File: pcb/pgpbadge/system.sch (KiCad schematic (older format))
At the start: 29 parts

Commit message: Board layout and routing done, need to fix DRC's, add more ground stitching, clean up silscreen, and review
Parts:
- added VIB+1: VIB+, pgpbadge:solder_pad, symbol Connector_Generic:Conn_01x01
- added VIB-1: VIB-, pgpbadge:solder_pad, symbol Connector_Generic:Conn_01x01
- gave numbers to parts that had none: 28
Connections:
- net En: now also C14.2, R16.2, U5.3 (EN)
- net GND: now also VIB-1.1 (Pin_1)
- net VIBPWM: now also VIB+1.1 (Pin_1)
- net GPOUT: no longer names the net of U5.27 (IO16)
- no-connect marks 13 -> 26

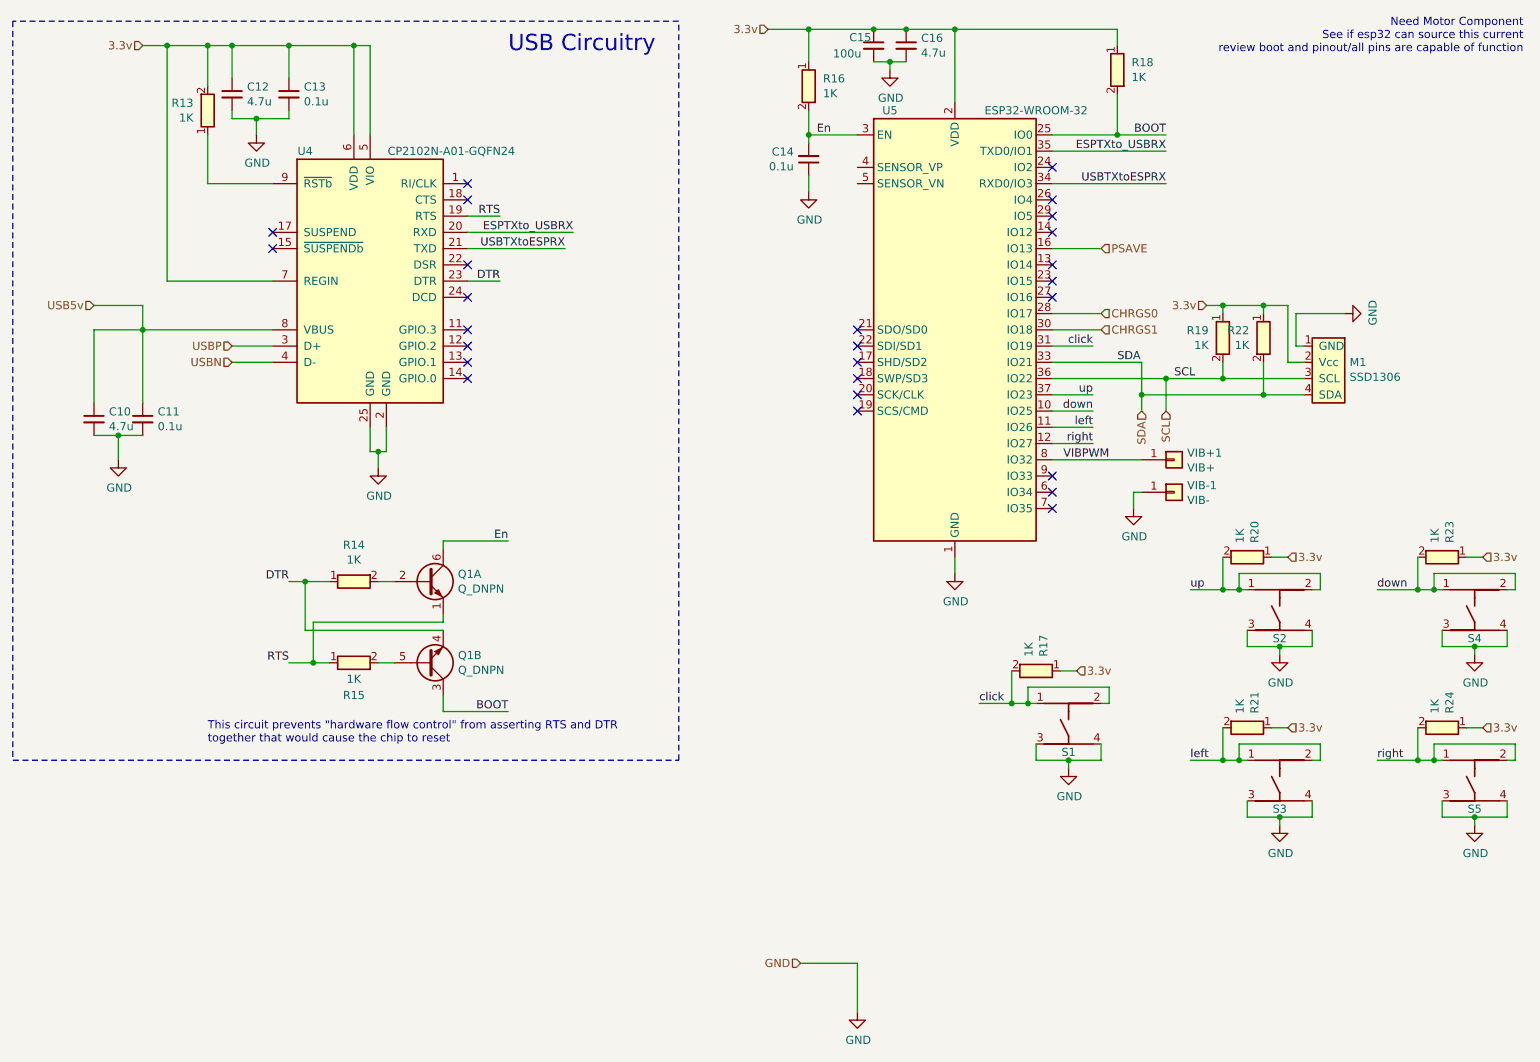
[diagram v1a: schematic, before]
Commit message: DRC's clean, silscreen updated, 1ks changed to 5.6k
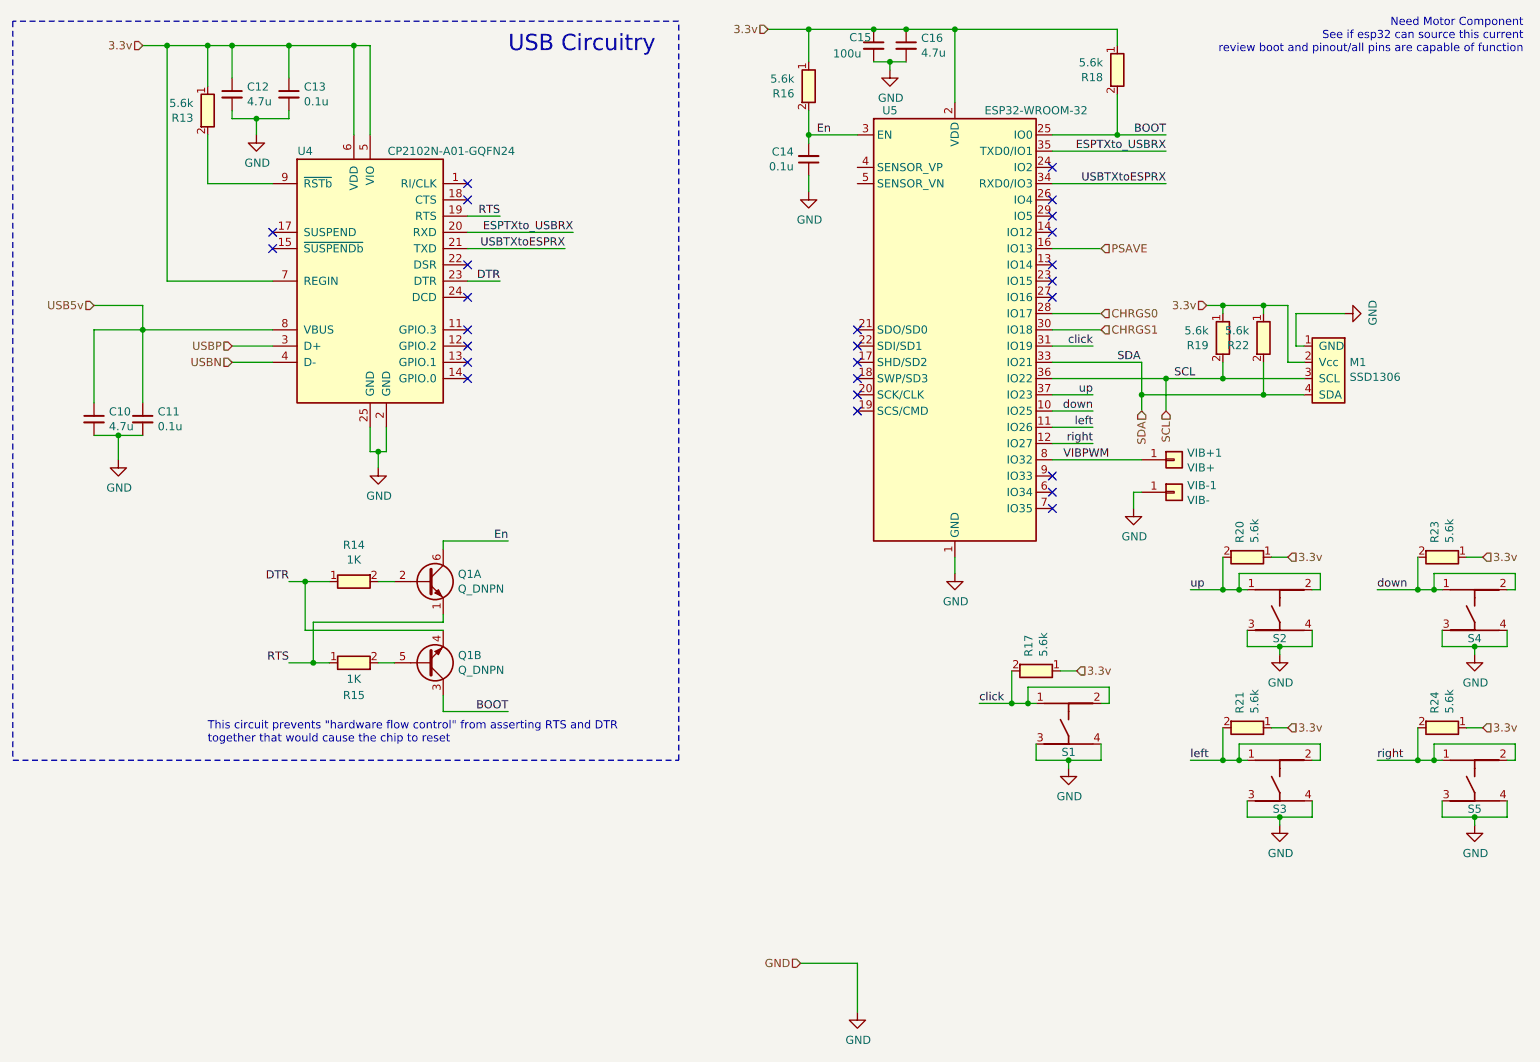
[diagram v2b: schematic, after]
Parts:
- R13, R16, R17, R18, R19, R20, R21, R22, R23, R24: value 1K -> 5.6k; DPN P1.00KLCT-ND -> P5.6KJCT-ND; PN ERJ-2RKF1001X -> ERJ-2GEJ562X; URL https://www.digikey.com/product-detail/en/panasonic-electronic-components/ERJ-2RKF1001X/P1-00KLCT-ND/97341 -> https://www.digikey.com/product-detail/en/panasonic-electronic-components/ERJ-2GEJ562X/P5-6KJCT-ND/147045
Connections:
- net 3.3v: now also R13.1; no longer R13.2
- net at U4.9 (~RSTb): now also R13.2; no longer R13.1
